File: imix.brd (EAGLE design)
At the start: 87 x 102.5 mm, 163 parts, among them IC1 AD712R, Q1 AO3418, Q2 AO3415, Q3 AO3415, Q5 AO3415, Q6 AO3415, U1 BQ2423X, U10 LDO-TPS78233, U11 ATSAM4LCX_100, U3 NRF51822, U4 BAL_NRF01D3, U6 FX0S8700CQ, U7 SI7021, U8 ISL29035, X1 16MHz, X2 16MHz, X4 16MHz

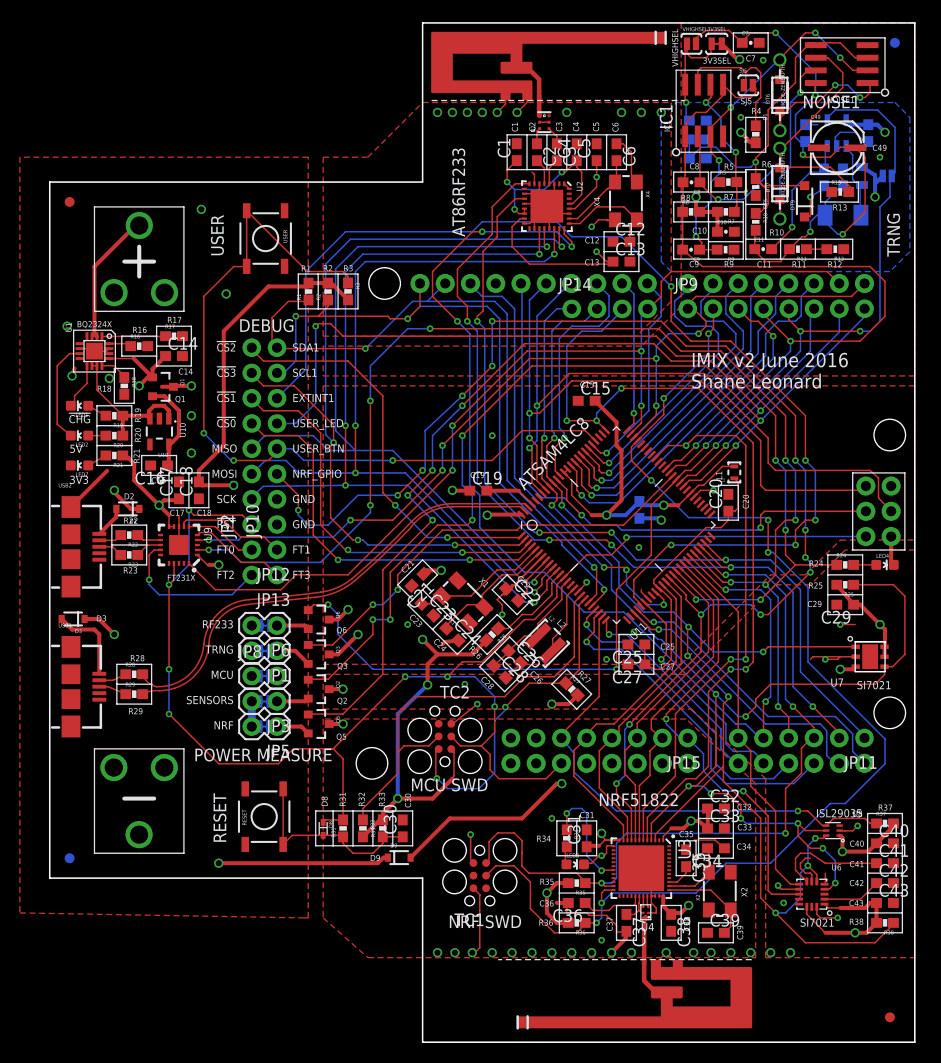
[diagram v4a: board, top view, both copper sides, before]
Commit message: Fix most assembly issues
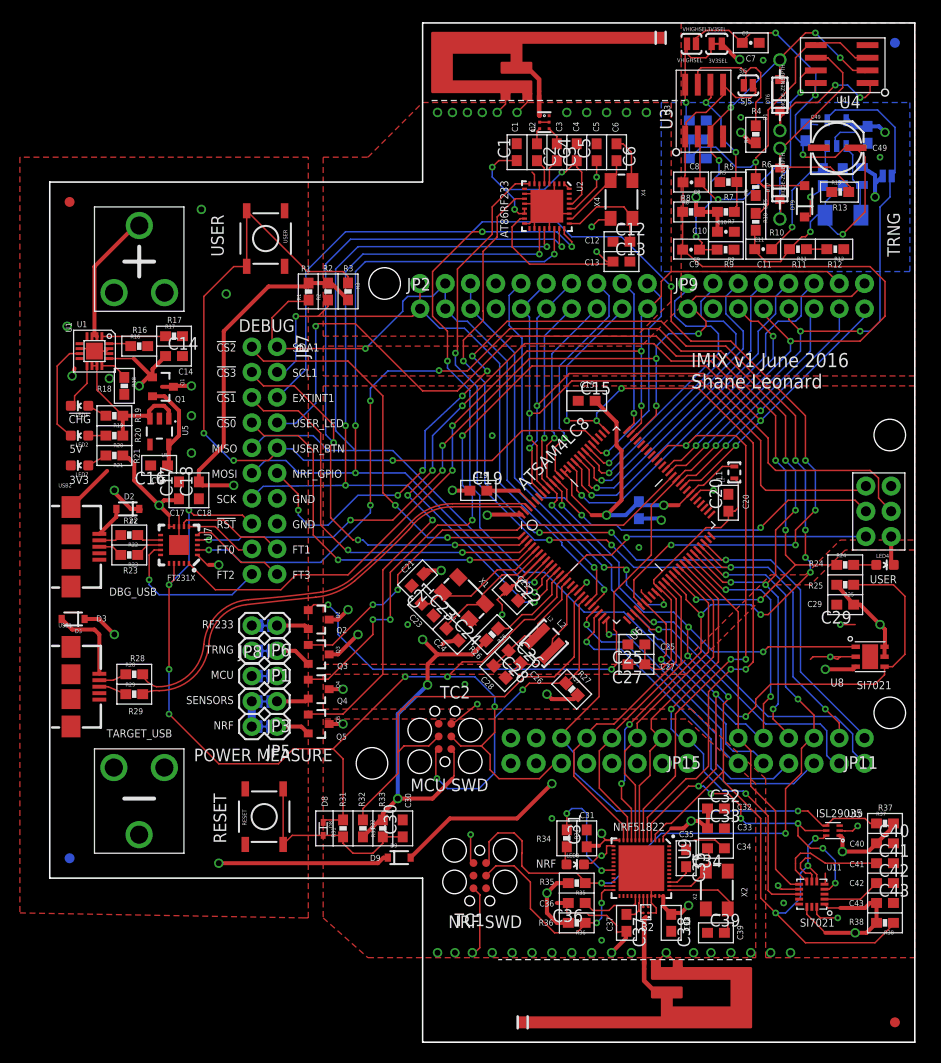
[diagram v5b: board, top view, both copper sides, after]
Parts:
- removed IC1, NOISE1: AD712R, analog-devices:SO8
- removed JP10: (no value), SparkFun-Connectors:1X08_NO_SILK
- removed JP12, JP13: (no value), SparkFun-Connectors:1X02_NO_SILK
- removed JP14: (no value), SparkFun-Connectors:1X04_NO_SILK_ALL_ROUND
- removed Q6: AO3415, SparkFun-DiscreteSemi:SOT23-3
- added B1: 2450BM15A0015, stanford_iot_research:BALUN0805
- added JP7: (no value), SparkFun-Connectors:2X10_ROUND_NOSILK
- added Q4: AO3415, SparkFun-DiscreteSemi:SOT23-3
- added U5: LDO-TPS78233, SparkFun-PowerIC:SOT23-5
- B2: value 2450BM15A0015 -> BAL_NRF01D3; device stanford_iot_research:BALUN0805 -> stanford_iot_research:BAL_NRF01D3
- JP2: device SparkFun-Connectors:1X08_NO_SILK -> SparkFun-Connectors:1X10_NO_SILK
- U10: value LDO-TPS78233 -> ISL29035; device SparkFun-PowerIC:SOT23-5 -> imix:ISL29035
- U11: value ATSAM4LCX_100 -> FX0S8700CQ; device imix:TQFP100 -> imix:QFN16_3,5
- U3: value NRF51822 -> AD712R; device imix:QFN48_6X6 -> analog-devices:SO8
- U4: value BAL_NRF01D3 -> AD712R; device stanford_iot_research:BAL_NRF01D3 -> analog-devices:SO8
- U6: value FX0S8700CQ -> ATSAM4LCX_100; device imix:QFN16_3,5 -> imix:TQFP100
- U7: value SI7021 -> (none); device imix:SI7021 -> stanford_iot_research:QFN20
- U8: value ISL29035 -> SI7021; device imix:ISL29035 -> imix:SI7021
- U9: value (none) -> NRF51822; device stanford_iot_research:QFN20 -> imix:QFN48_6X6
- moved U4 86.9 mm to (79.6, 81.9), turned to 90 degrees
- moved U10 78.7 mm to (78.8, 4.78)
- moved B2 78.2 mm to (59.4, -2.68), turned to 270 degrees
- moved U3 73.8 mm to (65.8, 77.2), turned to 0 degrees
- moved U7 70.4 mm to (13.0, 33.5), turned to 270 degrees
- moved U9 56.7 mm to (59.5, 1.00)
- moved U11 42.0 mm to (76.6, -1.61), turned to 180 degrees
- moved U6 42.0 mm to (57.0, 35.5), turned to 45 degrees
- moved JP2 27.5 mm to (37.2, 57.3), turned to 0 degrees
- moved U8 17.9 mm to (82.5, 22.3), turned to 0 degrees
- moved Q2 7.00 mm to (27.0, 26.0)
- moved U2 3.54 mm to (50.0, 67.6)
- moved X2 3.40 mm to (67.1, -1.20)
- moved X1 3.16 mm to (41.7, 28.1)
- moved X4 2.80 mm to (57.5, 68.2)
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- renumbered LT3 to L3
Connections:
- net !NRF_PWR_EN: now also U6.60; no longer U11.60
- net !RESET: now also JP7.15, U6.13, U7.4; no longer JP2.1, U11.13, U9.4
- net !RF233_PWR_EN: now also Q2.1, U6.61; no longer Q6.1, U11.61
- net !SENSE_PWR_EN: now also Q4.1, U6.59; no longer Q2.1, U11.59
- net !TRNG_PWR_EN: now also U6.62; no longer U11.62
- net ACC_INT1: now also U11.11, U6.42; no longer U11.42, U6.11
- net ACC_INT2: now also U11.9, U6.43; no longer U11.43, U6.9
- net ADCIFE0: now also U6.25; no longer U11.25
- net ADCIFE1: now also U6.31; no longer U11.31
- net ADCIFE2: now also U6.22; no longer U11.22
- net ADCIFE3: now also U6.23; no longer U11.23
- net ADCIFE4: now also U6.28; no longer U11.28
- net ADCIFE5: now also U6.29; no longer U11.29
- net AREF: now also JP2.3, U6.34; no longer U11.34
- net BIASH: now also U6.54; no longer U11.54
- net BIASL: now also U6.55; no longer U11.55
- net BUCK/BOOST: now also U6.12; no longer U11.12
- net BUFFER: now also U3.7; no longer IC1.7
- net EXTINT1: now also JP7.6, U6.30; no longer JP10.6, U11.30
- net FTDI0: now also JP7.17, U7.15; no longer JP12.2, U9.15
- net FTDI1: now also JP7.18, U7.14; no longer JP12.1, U9.14
- net FTDI2: now also JP7.19, U7.7; no longer JP13.2, U9.7
- net FTDI3: now also JP7.20, U7.16; no longer JP13.1, U9.16
- net GND: now also B1.2, B1.5, B1.6, B2.GND, JP2.4, JP7.14, JP7.16, JP9.2, U11.10, U11.12, U11.13, U11.16, U11.3, U11.5, U3.4, U4.4, U5.2, U5.4, U6.100, U6.15, U6.32, U6.33, U6.56, U7.13, U7.3, U7.PADDLE, U9.33, U9.34; no longer B2.2, B2.5, B2.6, IC1.4, JP10.1, JP10.2, NOISE1.4, U10.4, U11.100, U11.15, U11.32, U11.33, U11.56, U3.13, U3.33, U3.34, U3.PADDLE, U4.GND, U6.10, U6.12, U6.13, U6.16, U6.3, U6.5, U7.2, U9.3
- net GPIO2: now also U6.86; no longer U11.86
- net GPIO3: now also U6.85; no longer U11.85
- net GPIO4: now also U6.84; no longer U11.84
- net GPIO5: now also U6.83; no longer U11.83
- net GPIO6: now also U6.82; no longer U11.82
- net GPIO7: now also U6.81; no longer U11.81
- net GPIO8: now also U6.80; no longer U11.80
- net LIGHT_!INT: now also U10.4, U6.24; no longer U11.24, U8.4
- net MCU_VOUT3.3: now also U6.16; no longer U11.16
- net MISO: now also JP7.9, U6.9; no longer JP2.4, U11.9
- net MOSI: now also JP7.11, U6.10; no longer JP2.3, U11.10
- net N$10: now also U6.35; no longer U11.35
- net N$11: now also U6.6; no longer U11.6
- net N$12: now also U6.14; no longer U11.14
- net N$13: now also U6.5; no longer U11.5
- net N$15: now also U9.39; no longer U3.39
- net N$18: now also Q4.2; no longer Q2.2
- net N$19: now also U9.29; no longer U3.29
- net N$21: now also B2.DIFF@1, U9.31; no longer U3.31, U4.DIFF@1
- net N$22: now also B1.3; no longer B2.3
- net N$23: now also B2.DIFF@2, U9.32; no longer U3.32, U4.DIFF@2
- net N$24: now also U7.9; no longer U9.9
- net N$30: now also U7.8; no longer U9.8
- net N$37: now also Q2.2; no longer Q6.2
- net N$41: now also B1.4; no longer B2.4
- net N$42: now also B1.1; no longer B2.1
- net N$5: now also B2.SE; no longer U4.SE
- net N$51: now also U4.1; no longer NOISE1.1
- net N$52: now also U4.7; no longer NOISE1.7
- net N$6: now also B2.VCC, U9.30; no longer U3.30, U4.VCC
- net N$61: now also U11.8; no longer U6.8
- net N$62: now also U11.2; no longer U6.2
- net N$66: now also U4.3, U4.5; no longer NOISE1.3, NOISE1.5
- net N$67: now also U3.6; no longer IC1.6
- net N$68: now also U3.8; no longer IC1.8
- net N$7: now also U9.38; no longer U3.38
- net N$9: now also U9.37; no longer U3.37
- net NOISE1: now also U3.3, U4.2; no longer IC1.3, NOISE1.2
- net NOISE2: now also U3.2, U4.6; no longer IC1.2, NOISE1.6
- net NRF_GPIO: now also JP7.12, U6.38, U9.9; no longer JP10.3, U11.38, U3.9
- net NRF_INT: now also U6.67, U9.6; no longer U11.67, U3.6
- net NRF_LED: now also U9.19; no longer U3.19
- net NRF_SWDCLK: now also U9.24; no longer JP9.2, U11.72, U3.24
- net NRF_SWDIO: now also U6.46, U9.23; no longer U11.46, U3.23
- net RF233_!RST: now also U6.47; no longer U11.47
- net RF233_IRQ: now also U6.44; no longer U11.44
- net RF233_SLP: now also U6.48; no longer U11.48
- net SCK: now also JP7.13, U6.11; no longer JP2.2, U11.11
- net SPI_NCS0: now also JP7.7, U6.4; no longer JP2.5, U11.4
- net SPI_NCS1: now also JP7.5, U6.3; no longer JP2.6, U11.3
- net SPI_NCS2: now also JP7.1, U6.1; no longer JP2.8, U11.1
- net SPI_NCS3: now also JP7.3, U6.2; no longer JP2.7, U11.2
- net SWDCLK/TCK: now also U6.18; no longer U11.18
- net SWDIO/TMS: now also U6.19; no longer U11.19
- net TRNG_EN: now also U6.63; no longer U11.63
- net TRNG_OUT: now also U3.1, U3.5, U6.64; no longer IC1.1, IC1.5, U11.64
- net TWI1_SCL: now also JP2.1, JP7.4, U6.21; no longer JP10.7, U11.21
- net TWI1_SDA: now also JP2.2, JP7.2, U6.20; no longer JP10.8, U11.20
- net TWI2_SCL: now also JP2.7, U10.5, U11.4, U6.92, U8.6, U9.4; no longer JP14.1, U11.92, U3.4, U6.4, U7.6, U8.5
- net TWI2_SDA: now also JP2.8, U10.6, U11.6, U6.91, U8.1, U9.3; no longer JP14.2, U11.91, U3.3, U6.6, U7.1, U8.6
- net USART0_CLK: now also U6.90; no longer U11.90
- net USART0_CTS: now also U6.75; no longer U11.75
- net USART0_RTS: now also U6.89; no longer U11.89
- net USART0_RX: now also JP2.5, U6.93; no longer U11.93
- net USART0_TX: now also JP2.6, U6.94; no longer U11.94
- net USART2_CLK: now also JP2.9, U6.76, U9.5; no longer JP14.3, U11.76, U3.5
- net USART2_CTS: now also U6.37, U9.10; no longer U11.37, U3.10
- net USART2_RTS: now also U6.36, U9.11; no longer U11.36, U3.11
- net USART2_RX: now also U6.40, U9.8; no longer U11.40, U3.8
- net USART2_TX: now also U6.41, U9.7; no longer U11.41, U3.7
- net USART3_RTS: now also U6.45, U7.19; no longer U11.45, U9.19
- net USART3_RX: now also U6.73, U7.17; no longer U11.73, U9.17
- net USART3_TX: now also JP2.10, U6.74, U7.1; no longer JP14.4, U11.74, U9.1
- net USB_N: now also U6.98; no longer U11.98
- net USB_P: now also U6.99; no longer U11.99
- net USER_BTN: now also JP7.10, U6.79; no longer JP10.4, U11.79
- net USER_LED: now also JP7.8, U6.39; no longer JP10.5, U11.39
- net VCC: now also U5.5; no longer U10.5
- net VCC_3V3: now also U7.11, U7.12, U7.20; no longer U9.11, U9.12, U9.20
- net VCC_LDO: now also U5.1, U5.3; no longer U10.1, U10.3
- net VCC_MCU_3V3: now also U6.17, U6.57, U6.8, U6.87, U6.88, U6.97; no longer U11.17, U11.57, U11.8, U11.87, U11.88, U11.97
- net VCC_NRF_3V3: now also U9.1, U9.12, U9.35, U9.36; no longer U3.1, U3.12, U3.35, U3.36
- net VCC_RF233_3V3: now also Q2.3; no longer Q6.3
- net VCC_SENSE_3V3: now also Q4.3, U10.1, U11.1, U11.14, U8.3, U8.4, U8.5; no longer Q2.3, U6.1, U6.14, U7.3, U7.4, U7.5, U8.1
- net VHIGH: now also U4.8; no longer NOISE1.8
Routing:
- net NRF_SWDCLK: track 120.0 -> 21.1 mm, vias 7 -> 2
- net VCC_TRNG_3V3: track 102.7 -> 96.6 mm
- net USER_LED: track 97.6 -> 102.2 mm
- net TWI1_SCL: track 68.5 -> 64.0 mm, vias 3 -> 2
- net N$2: track 20.0 -> 23.3 mm
- net NRF_SWDIO: track 79.6 -> 77.5 mm
- net GND: track 156.6 -> 154.6 mm
- net TWI2_SCL: track 127.5 -> 125.8 mm
- net TWI1_SDA: track 69.4 -> 67.7 mm
- net USART0_RTS: track 24.3 -> 22.7 mm
- net TWI2_SDA: track 131.4 -> 129.9 mm
- net USART3_RTS: track 125.8 -> 124.4 mm
- net USART0_CLK: track 62.5 -> 63.7 mm
- net AREF: track 45.4 -> 44.2 mm
- net RF233_SLP: track 88.6 -> 89.7 mm
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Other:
- board text added: "!RF233_RST"
- board text added: "A0"
- board text added: "A1"
- board text added: "A2"
- board text added: "A3"
- board text added: "A4"
- board text added: "A5"
- board text added: "ACC_INT1"
- board text added: "C44"
- board text added: "C45"
- board text added: "C46"
- board text added: "C47"
- board text added: "C48"
- board text added: "C50"
- board text added: "CTS2"
- board text added: "DBG_USB"
- board text added: "IC2"
- board text added: "IMIX v1 June 2016 Shane Leonard"
- board text added: "IOREF"
- board text added: "L3"
- board text added: "LIGHT_INT"
- board text added: "NC"
- board text added: "NRF_SWDIO"
- board text added: "Q4"
- board text added: "R14"
- board text added: "R15"
- board text added: "RF233_IRQ"
- board text added: "RF233_SLP"
- board text added: "RTS2"
- board text added: "RTS3"
- board text added: "RX2"
- board text added: "SJ6"
- board text added: "TARGET_USB"
- board text added: "TX2"
- board text added: "U1"
- board text added: "U3"
- board text added: "U4"
- board text added: "U5"
- board text added: "VIN"
- board text removed: "!NRF_RST"
- board text removed: "BQ2324X"
- board text removed: "IC1"
- board text removed: "IMIX v2 June 2016 Shane Leonard"
- board text removed: "NOISE1"
- board text removed: "Q6"
- board text removed: "U10"

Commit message: Fix reset connection to FTDI
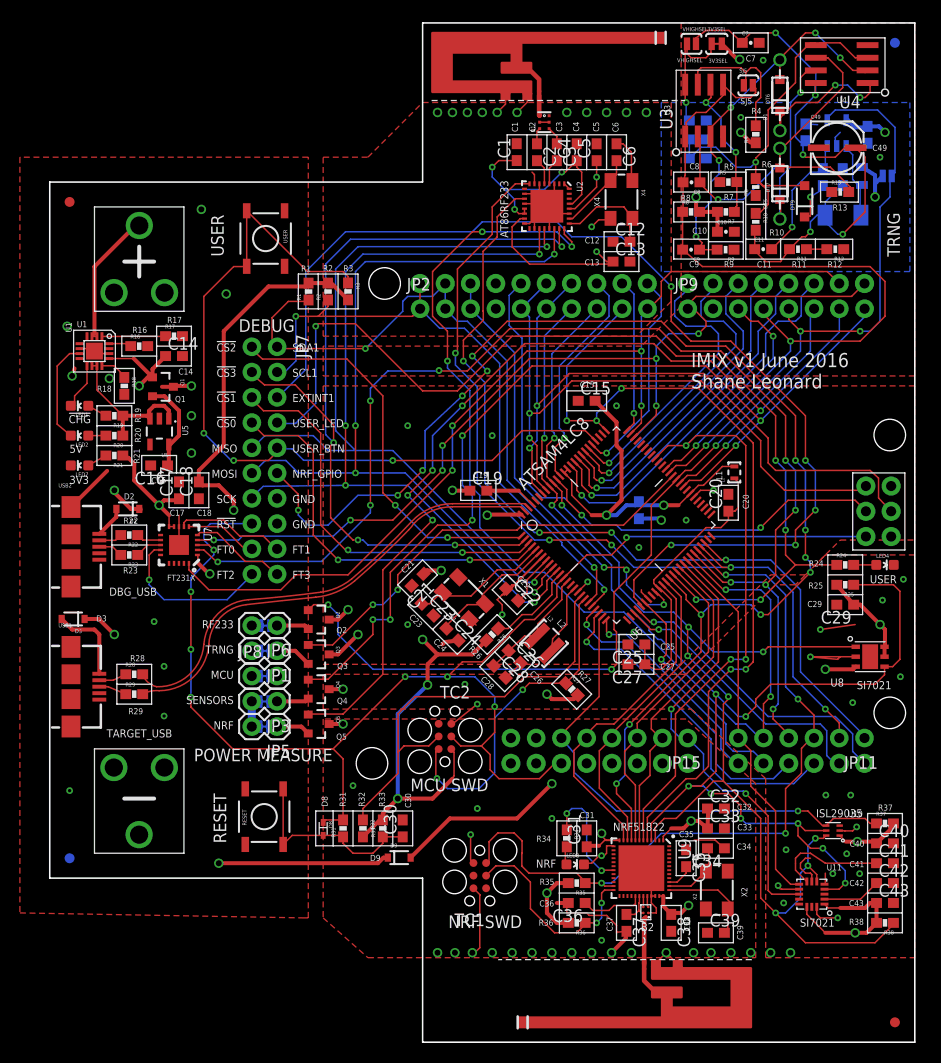
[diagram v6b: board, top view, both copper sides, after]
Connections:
- net !RESET: now also U7.18; no longer U7.4
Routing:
- net !RESET: track 148.2 -> 140.6 mm
- net TWI2_SCL: track 125.8 -> 127.9 mm
- net VCC_SENSE_3V3: track 91.7 -> 90.2 mm
- net USART0_RX: track 65.4 -> 64.3 mm
- net VCC_MCU_3V3: track 166.4 -> 165.6 mm
- net GND: track 154.6 -> 154.4 mm, vias 61 -> 80

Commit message: Update component naming for consistency
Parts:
- removed X4: 16MHz, stanford_iot_research:CTS_405_SERIES
- added X3: 16MHz, stanford_iot_research:CTS_405_SERIES
- C49: value (none) -> 10uF
- L3: value (none) -> 10uH
- moved X1 43.1 mm to (57.5, 68.2), turned to 270 degrees
- moved X2 38.8 mm to (41.7, 28.1), turned to 135 degrees
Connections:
- net GND: now also X3.CASE@2, X3.CASE@4; no longer X4.CASE@2, X4.CASE@4
- net N$11: now also X2.1; no longer X1.1
- net N$13: now also X2.3; no longer X1.3
- net N$4: now also X1.1; no longer X4.1
- net N$40: now also X1.3; no longer X4.3
- net N$7: now also X3.3; no longer X2.3
- net N$9: now also X3.1; no longer X2.1
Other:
- board text added: "B1"
- board text added: "FX0S8700CQ"
- board text added: "X3"
- board text removed: "X4"
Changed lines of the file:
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@@
 <wire x1="84" y1="79.5" x2="84" y2="84.5" width="0.1" layer="21"/>
 <wire x1="84" y1="84.5" x2="75.5" y2="84.5" width="0.1" layer="21"/>
-<text x="84.65" y="19.81" size="0.8128" layer="21" font="vector" rot="R180">SI7021</text>
-<text x="78.93" y="-4.07" size="0.8128" layer="21" font="vector" rot="R180">SI7021</text>
-<text x="81.75" y="6.93" size="0.8128" layer="21" font="vector" rot="R180">ISL29035</text>
+<text x="84.15" y="19.81" size="0.6096" layer="21" font="vector" rot="R180">SI7021</text>
+<text x="78.43" y="-4.07" size="0.6096" layer="21" font="vector" rot="R180">FX0S8700CQ</text>
+<text x="80.75" y="6.93" size="0.6096" layer="21" font="vector" rot="R180">ISL29035</text>
 <text x="46.48" y="76.04" size="0.6096" layer="21" font="vector" rot="R270">C1</text>
 <text x="48.23" y="76.05" size="0.6096" layer="21" font="vector" rot="R270">C2</text>
@@
 <text x="66.1" y="65.42" size="0.6096" layer="21" font="vector" rot="R180">C10</text>
 <text x="69.46" y="77.83" size="0.6096" layer="21" font="vector">SJ5</text>
-<text x="55.35" y="67.5" size="0.6096" layer="21" font="vector" rot="R90">X4</text>
+<text x="55.35" y="67.5" size="0.6096" layer="21" font="vector" rot="R90">X1</text>
 <text x="53.31" y="49.33" size="0.6096" layer="21" font="vector">C15</text>
 <text x="67.63" y="40.05" size="0.6096" layer="21" font="vector" rot="R90">L1</text>
@@
 <text x="56.61" y="-5.37" size="0.6096" layer="21" font="vector" rot="R90">C37</text>
 <text x="69.74" y="-6.22" size="0.6096" layer="21" font="vector" rot="R90">C39</text>
-<text x="70.16" y="-1.91" size="0.6096" layer="21" font="vector" rot="R90">X2</text>
+<text x="70.16" y="-1.91" size="0.6096" layer="21" font="vector" rot="R90">X3</text>
 <text x="25.28" y="61" size="0.6096" layer="21" font="vector">R1</text>
 <text x="27.48" y="61.03" size="0.6096" layer="21" font="vector">R2</text>
@@
 <text x="50.95" y="25.66" size="0.6096" layer="21" font="vector" rot="R315">L2</text>
 <text x="53.05" y="20.51" size="0.6096" layer="21" font="vector" rot="R315">R27</text>
-<text x="43.11" y="29.85" size="0.6096" layer="21" font="vector" rot="R315">X1</text>
+<text x="43.11" y="29.85" size="0.6096" layer="21" font="vector" rot="R315">X2</text>
 <text x="48.21" y="20.5" size="0.6096" layer="21" font="vector" rot="R315">C26</text>
 <wire x1="9" y1="63.5" x2="9" y2="60.5" width="0.4064" layer="21"/>
@@
 <text x="40.16" y="55.96" size="0.8128" layer="22" font="vector" rot="MR270">SDA1</text>
 <text x="37.62" y="55.96" size="0.8128" layer="22" font="vector" rot="MR270">SCL1</text>
+<text x="49.24" y="77.42" size="0.6096" layer="21" font="vector">B1</text>
 </plain>
 <attributes>
@@
 <element name="C48" library="SparkFun-Capacitors" package="0603-CAP" value="" x="82.25" y="74.75" rot="MR270"/>
 <element name="C8" library="SparkFun-Capacitors" package="0603-CAP" value="" x="64.54" y="69.975" rot="R180"/>
-<element name="C49" library="SparkFun-Capacitors" package="PANASONIC_C" value="" x="79.145" y="73.65"/>
+<element name="C49" library="SparkFun-Capacitors" package="PANASONIC_C" value="10uF" x="79.145" y="73.65"/>
 <element name="C46" library="SparkFun-Passives" package="0603-CAP" value="" x="65.175" y="72.38" rot="MR180"/>
 <element name="C23" library="rcl" package="C0603" value="13pF" x="38" y="27" rot="R315"/>
@@
 <attribute name="PROD_ID" value="DIO-00821" x="3" y="41.5" size="1.778" layer="27" rot="R90" display="off"/>
 </element>
-<element name="L3" library="SparkFun-Passives" package="0805" value="" x="81.685" y="70.61" rot="MR90"/>
+<element name="L3" library="SparkFun-Passives" package="0805" value="10uH" x="81.685" y="70.61" rot="MR90"/>
 <element name="U4" library="analog-devices" package="SO8" value="AD712R" x="79.645" y="81.865" rot="R90">
 <attribute name="MF" value="ALTERA CORPORATION" x="79.645" y="81.865" size="1.778" layer="27" rot="R90" display="off"/>
@@
 </element>
 <element name="VHIGHSEL" library="SparkFun-Retired" package="SJ_2S-NO" value="SOLDERJUMPER-OLDNO" x="64.54" y="83.905"/>
-<element name="X1" library="stanford_iot_research" package="CTS_405_SERIES" value="16MHz" x="41.66" y="28.14" rot="R135"/>
-<element name="X2" library="stanford_iot_research" package="CTS_405_SERIES" value="16MHz" x="67.086" y="-1.2" rot="R90"/>
-<element name="X4" library="stanford_iot_research" package="CTS_405_SERIES" value="16MHz" x="57.5" y="68.25" rot="R270"/>
+<element name="X2" library="stanford_iot_research" package="CTS_405_SERIES" value="16MHz" x="41.66" y="28.14" rot="R135"/>
+<element name="X3" library="stanford_iot_research" package="CTS_405_SERIES" value="16MHz" x="67.086" y="-1.2" rot="R90"/>
+<element name="X1" library="stanford_iot_research" package="CTS_405_SERIES" value="16MHz" x="57.5" y="68.25" rot="R270"/>
 <element name="JP8" library="SparkFun-Connectors" package="1X02" value="" x="20.32" y="20.32"/>
 <element name="JP11" library="SparkFun-Connectors" package="1X06_NO_SILK" value="" x="81.94" y="14.088" rot="R180">
@@
 <contactref element="C23" pad="2"/>
 <contactref element="C24" pad="2"/>
-<contactref element="X1" pad="CASE@2"/>
-<contactref element="X1" pad="CASE@4"/>
+<contactref element="X2" pad="CASE@2"/>
+<contactref element="X2" pad="CASE@4"/>
 <contactref element="C21" pad="2"/>
 <contactref element="LED4" pad="C"/>
@@
 <contactref element="C31" pad="2"/>
 <contactref element="C38" pad="2"/>
-<contactref element="X2" pad="CASE@2"/>
-<contactref element="X2" pad="CASE@4"/>
+<contactref element="X3" pad="CASE@2"/>
+<contactref element="X3" pad="CASE@4"/>
 <contactref element="LED3" pad="C"/>
 <contactref element="C33" pad="2"/>
@@
 <wire x1="79.145" y1="73.6199" x2="79.145" y2="73.855" width="0.1524" layer="16"/>
 <wire x1="76" y1="75.85" x2="77.23" y2="75.77" width="0.1524" layer="16"/>
-<contactref element="X4" pad="CASE@2"/>
-<contactref element="X4" pad="CASE@4"/>
+<contactref element="X1" pad="CASE@2"/>
+<contactref element="X1" pad="CASE@4"/>
 <contactref element="C12" pad="1"/>
 <contactref element="C6" pad="1"/>
@@
 <signal name="N$11">
 <contactref element="C24" pad="1"/>
-<contactref element="X1" pad="1"/>
+<contactref element="X2" pad="1"/>
 <contactref element="U6" pad="6"/>
 <wire x1="49.221825" y1="32.671571875" x2="49.171571875" y2="32.671571875" width="0.1524" layer="1"/>
@@
 <signal name="N$13">
 <contactref element="C23" pad="1"/>
-<contactref element="X1" pad="3"/>
+<contactref element="X2" pad="3"/>
 <contactref element="U6" pad="5"/>
 <wire x1="48.868271875" y1="33.025125" x2="46.843146875" y2="31" width="0.1524" layer="1"/>
@@
 <signal name="N$40">
 <contactref element="C12" pad="2"/>
-<contactref element="X4" pad="3"/>
+<contactref element="X1" pad="3"/>
 <contactref element="U2" pad="25"/>
 <wire x1="52.247" y1="65.824" x2="53.324" y2="65.824" width="0.1524" layer="1"/>
@@
 <wire x1="53.5" y1="68.75" x2="53.5" y2="71" width="0.1524" layer="1"/>
 <wire x1="53.5" y1="71" x2="53" y2="71.5" width="0.1524" layer="1"/>
-<wire x1="53" y1="72.15" x2="51.85" y2="71" width="0.1524" layer="1"/>
-<wire x1="51.85" y1="71" x2="51.5" y2="71" width="0.1524" layer="1"/>
-<via x="51.5" y="71" extent="1-16" drill="0.3302"/>
-<wire x1="51.5" y1="71" x2="49.75" y2="69.25" width="0.1524" layer="16"/>
-<wire x1="49.75" y1="69.25" x2="45.75" y2="69.25" width="0.1524" layer="16"/>
+<wire x1="53" y1="72.15" x2="52.15" y2="71" width="0.1524" layer="1"/>
+<wire x1="52.15" y1="71" x2="52" y2="71" width="0.1524" layer="1"/>
+<via x="52" y="71" extent="1-16" drill="0.3302"/>
+<wire x1="52" y1="71" x2="50.25" y2="69.25" width="0.1524" layer="16"/>
+<wire x1="50.25" y1="69.25" x2="45.75" y2="69.25" width="0.1524" layer="16"/>
 <wire x1="53" y1="71.5" x2="53" y2="72.15" width="0.1524" layer="1"/>
 <wire x1="46.965" y1="72.16" x2="45.16" y2="72.16" width="0.1524" layer="1"/>
@@
 <contactref element="U2" pad="26"/>
 <contactref element="C6" pad="2"/>
-<contactref element="X4" pad="1"/>
+<contactref element="X1" pad="1"/>
 <wire x1="52.247" y1="66.324" x2="52.574" y2="66.324" width="0.1524" layer="1"/>
 <wire x1="52.574" y1="66.324" x2="56.4" y2="70.15" width="0.1524" layer="1"/>
@@
 <signal name="N$7">
 <contactref element="C34" pad="2"/>
-<contactref element="X2" pad="3"/>
+<contactref element="X3" pad="3"/>
 <contactref element="U9" pad="38"/>
 <wire x1="62.3" y1="-0.8" x2="64.486" y2="-0.8" width="0.1524" layer="1"/>
@@
 <signal name="N$9">
 <contactref element="C39" pad="2"/>
-<contactref element="X2" pad="1"/>
+<contactref element="X3" pad="1"/>
 <contactref element="U9" pad="37"/>
 <wire x1="62.3" y1="-1.2" x2="67.2" y2="-1.2" width="0.1524" layer="1"/>
